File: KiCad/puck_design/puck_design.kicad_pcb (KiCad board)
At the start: 2 copper layers, 49.4 x 55.9 mm, 28 parts, among them J1 SJ-2523-SMT-TR, Q1 CSD16406Q3, Q2 CSD16406Q3, U1 ITG-3701, U2 BT840F, U3 TE832-M1, U4 MCP73832-2, U5 BQ29700DSER

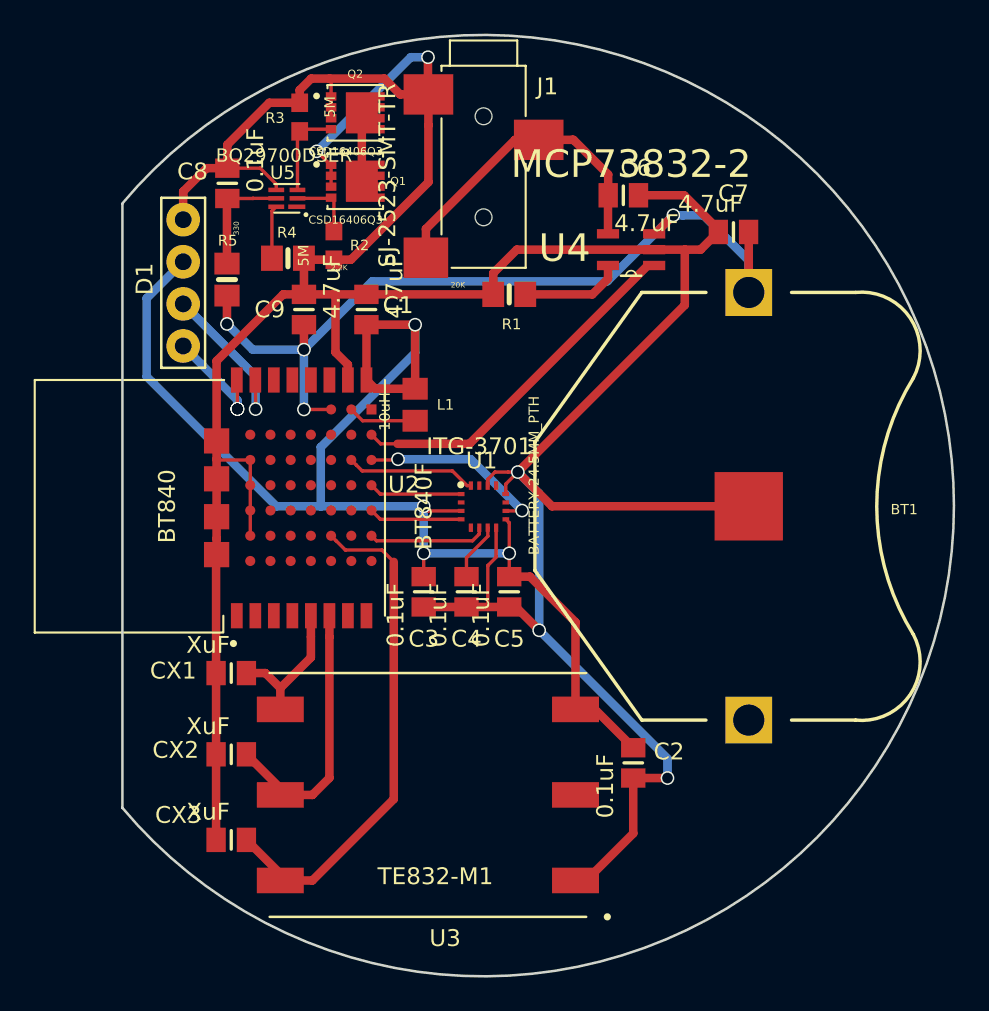
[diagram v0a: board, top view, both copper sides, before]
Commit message: Added mounting holes and updated gerber/drill files
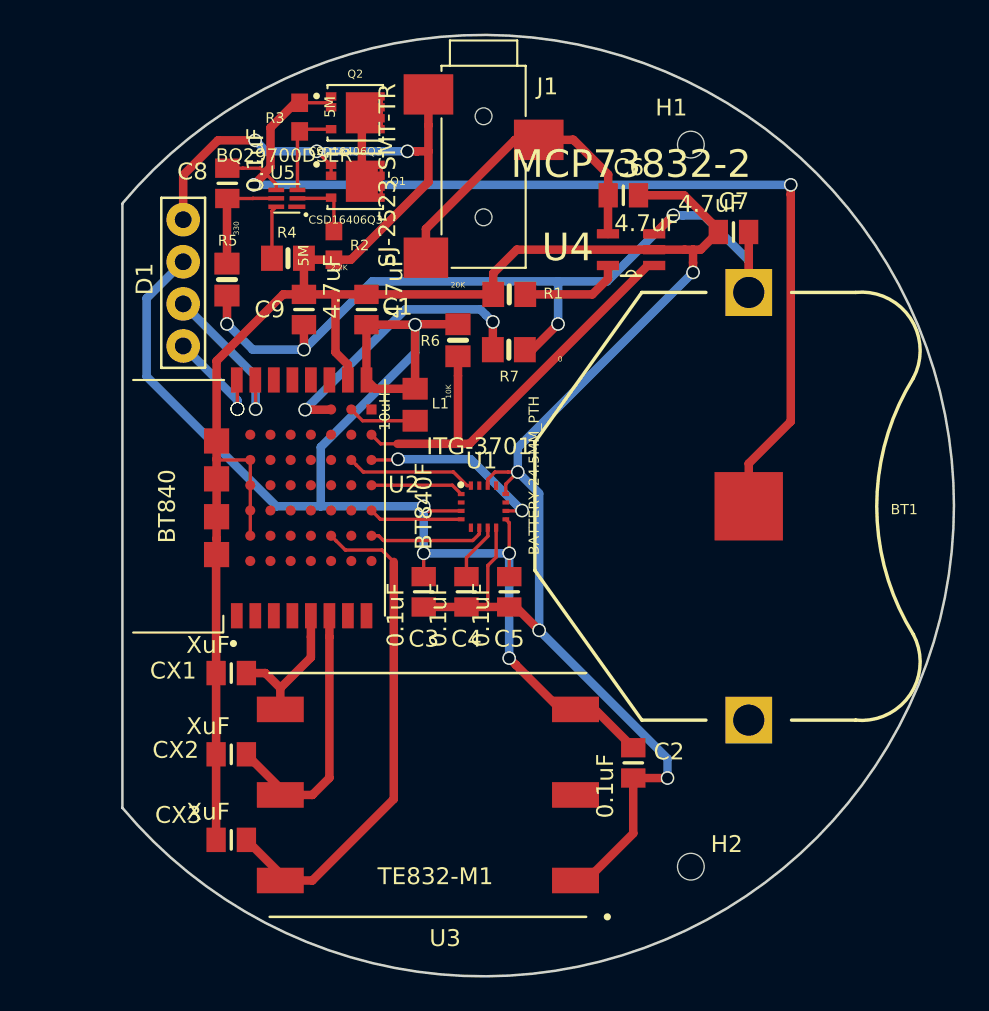
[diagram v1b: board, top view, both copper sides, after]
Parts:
- added H1: Mounting Hole, puck_footprints:Mounting Hole, F.Cu at (162.3, 77.2)
- added H2: Mounting Hole, puck_footprints:Mounting Hole, F.Cu at (163.5, 119.2)
- added R6: 10K, puck_footprints:0805-NO, F.Cu at (148.5, 90.1)
- added R7: 0, puck_footprints:0805-NO, F.Cu at (151.5, 90.7)
- U4: footprint puck_footprints:MCP73831T_2ATI_OT -> puck_footprints:MCP73832T_2ATI_OT
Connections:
- BT1 pad 2: GND -> Net-(BT1-Pad2)
- C8 pad 2: GND -> Net-(BT1-Pad2)
- Q2 pad 1: GND -> Net-(BT1-Pad2)
- Q2 pad 2: GND -> Net-(BT1-Pad2)
- R3 pad 2: GND -> Net-(BT1-Pad2)
- U1 pad 11: Net-(U1-Pad11) -> (no net)
- U1 pad 13: Net-(U1-Pad13) -> (no net)
- U1 pad 15: Net-(U1-Pad15) -> (no net)
- U1 pad 2: Net-(U1-Pad2) -> (no net)
- U1 pad 5: Net-(U1-Pad5) -> (no net)
- U2 pad 1: Net-(U2-Pad1) -> (no net)
- U2 pad 11: Net-(U2-Pad11) -> (no net)
- U2 pad 12: Net-(U2-Pad12) -> (no net)
- U2 pad 13: Net-(U2-Pad13) -> (no net)
- U2 pad 14: Net-(U2-Pad14) -> (no net)
- U2 pad 2: Net-(U2-Pad2) -> (no net)
- U2 pad 3: Net-(U2-Pad3) -> (no net)
- U2 pad 4: Net-(U2-Pad4) -> (no net)
- U2 pad 7: Net-(U2-Pad7) -> (no net)
- U2 pad 8: Net-(U2-Pad8) -> (no net)
- U2 pad A1: Net-(U2-PadA1) -> (no net)
- U2 pad A2: Net-(U2-PadA2) -> (no net)
- U2 pad A3: Net-(U2-PadA3) -> (no net)
- U2 pad A5: Net-(U2-PadA5) -> (no net)
- U2 pad B1: Net-(U2-PadB1) -> (no net)
- U2 pad B2: Net-(U2-PadB2) -> (no net)
- U2 pad B3: Net-(U2-PadB3) -> (no net)
- U2 pad B4: Net-(U2-PadB4) -> (no net)
- U2 pad B5: Net-(U2-PadB5) -> (no net)
- U2 pad C1: Net-(U2-PadC1) -> (no net)
- U2 pad C2: Net-(U2-PadC2) -> (no net)
- U2 pad C3: Net-(U2-PadC3) -> (no net)
- U2 pad C4: Net-(U2-PadC4) -> (no net)
- U2 pad C5: Net-(U2-PadC5) -> (no net)
- U2 pad D1: Net-(U2-PadD1) -> (no net)
- U2 pad D2: Net-(U2-PadD2) -> (no net)
- U2 pad D3: Net-(U2-PadD3) -> (no net)
- U2 pad D4: Net-(U2-PadD4) -> (no net)
- U2 pad E0: Net-(U2-PadE0) -> (no net)
- U2 pad E1: Net-(U2-PadE1) -> (no net)
- U2 pad E2: Net-(U2-PadE2) -> (no net)
- U2 pad E3: Net-(U2-PadE3) -> (no net)
- U2 pad E4: Net-(U2-PadE4) -> (no net)
- U2 pad E5: Net-(U2-PadE5) -> (no net)
- U2 pad F4: +BATT -> Net-(R7-Pad1)
- U2 pad F6: Net-(U2-PadF6) -> (no net)
- U2 pad Z0: Net-(U2-PadZ0) -> (no net)
- U2 pad Z1: Net-(U2-PadZ1) -> (no net)
- U2 pad Z2: Net-(U2-PadZ2) -> (no net)
- U2 pad Z3: Net-(U2-PadZ3) -> (no net)
- U2 pad Z4: Net-(U2-PadZ4) -> (no net)
- U2 pad Z5: Net-(U2-PadZ5) -> (no net)
- U2 pad Z6: Net-(U2-PadZ6) -> (no net)
- U3 pad 2: Net-(U3-Pad2) -> (no net)
- U5 pad 1: Net-(U5-Pad1) -> (no net)
- U5 pad 4: GND -> Net-(BT1-Pad2)
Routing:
- net Net-(BT1-Pad2): track 0.00 -> 64.3 mm, vias 0 -> 2
- net GND: track 216.8 -> 182.3 mm, vias 5 -> 7
- net Net-(R7-Pad1): track 0.00 -> 17.1 mm, vias 0 -> 2
- net Net-(Q1-Pad9): track 4.06 -> 12.0 mm
- net Net-(R6-Pad2): track 21.4 -> 26.6 mm
- net VCC: track 83.4 -> 87.1 mm, vias 4 -> 5
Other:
- net class Default: clearance 0.25 -> 0.1016
- net class temp added: clearance 0.1016, trace_width 0.1524, via_dia 0.8128, via_drill 0.635
- rule trace_clearance: 0.25 -> 0.1016
- rule trace_min: 0.1016 -> 0
- board text added: "Team 2 Performance Tracking Hockey Puck"
